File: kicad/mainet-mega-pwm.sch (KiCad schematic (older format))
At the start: 0 parts

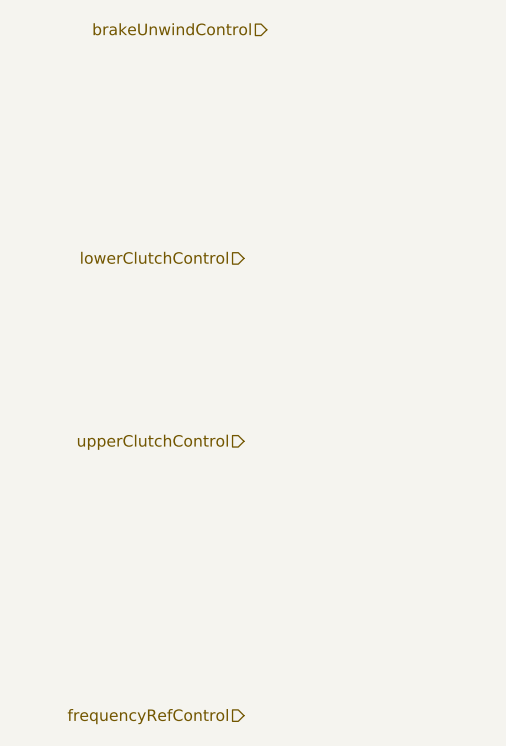
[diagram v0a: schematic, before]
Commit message: Kicad: Modificaciones menores esquemáticos
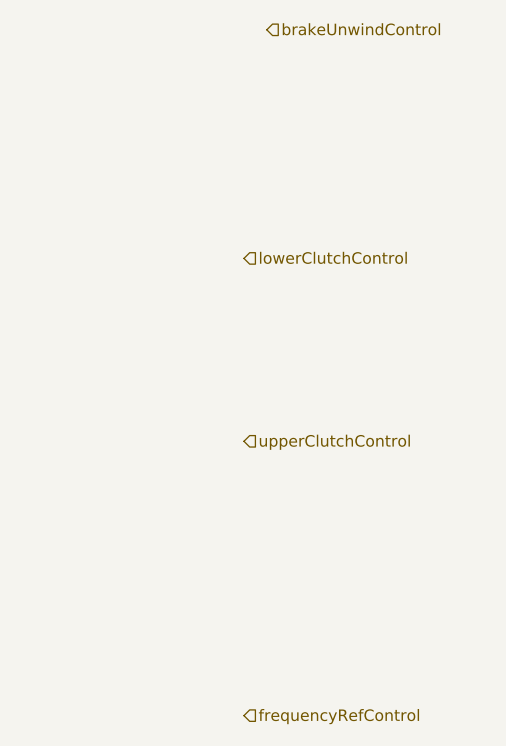
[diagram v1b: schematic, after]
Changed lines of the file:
@@
 $Descr A4 11693 8268
 encoding utf-8
-Sheet 3 17
+Sheet 17 17
 Title ""
 Date ""
@@
 Comment4 ""
 $EndDescr
-Text HLabel 2350 1700 0    50   Input ~ 0
+Text HLabel 2350 1700 2    50   Input ~ 0
 brakeUnwindControl
-Text HLabel 2250 2700 0    50   Input ~ 0
+Text HLabel 2250 2700 2    50   Input ~ 0
 lowerClutchControl
-Text HLabel 2250 3500 0    50   Input ~ 0
+Text HLabel 2250 3500 2    50   Input ~ 0
 upperClutchControl
-Text HLabel 2250 4700 0    50   Input ~ 0
+Text HLabel 2250 4700 2    50   Input ~ 0
 frequencyRefControl
 $EndSCHEMATC

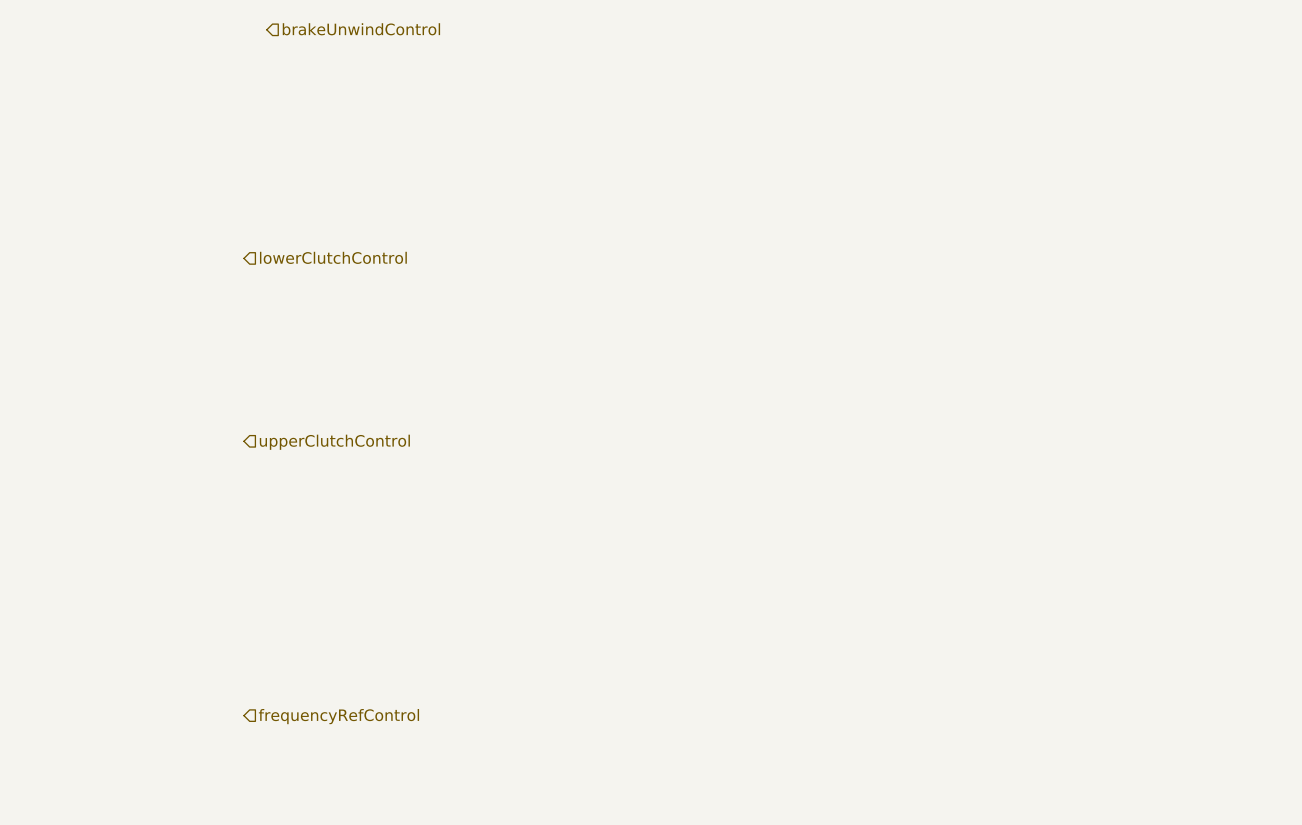
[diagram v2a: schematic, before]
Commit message: KiCAD: Se agregó esquemáticos del módulo de coversión de voltaje de 5V a !0 V
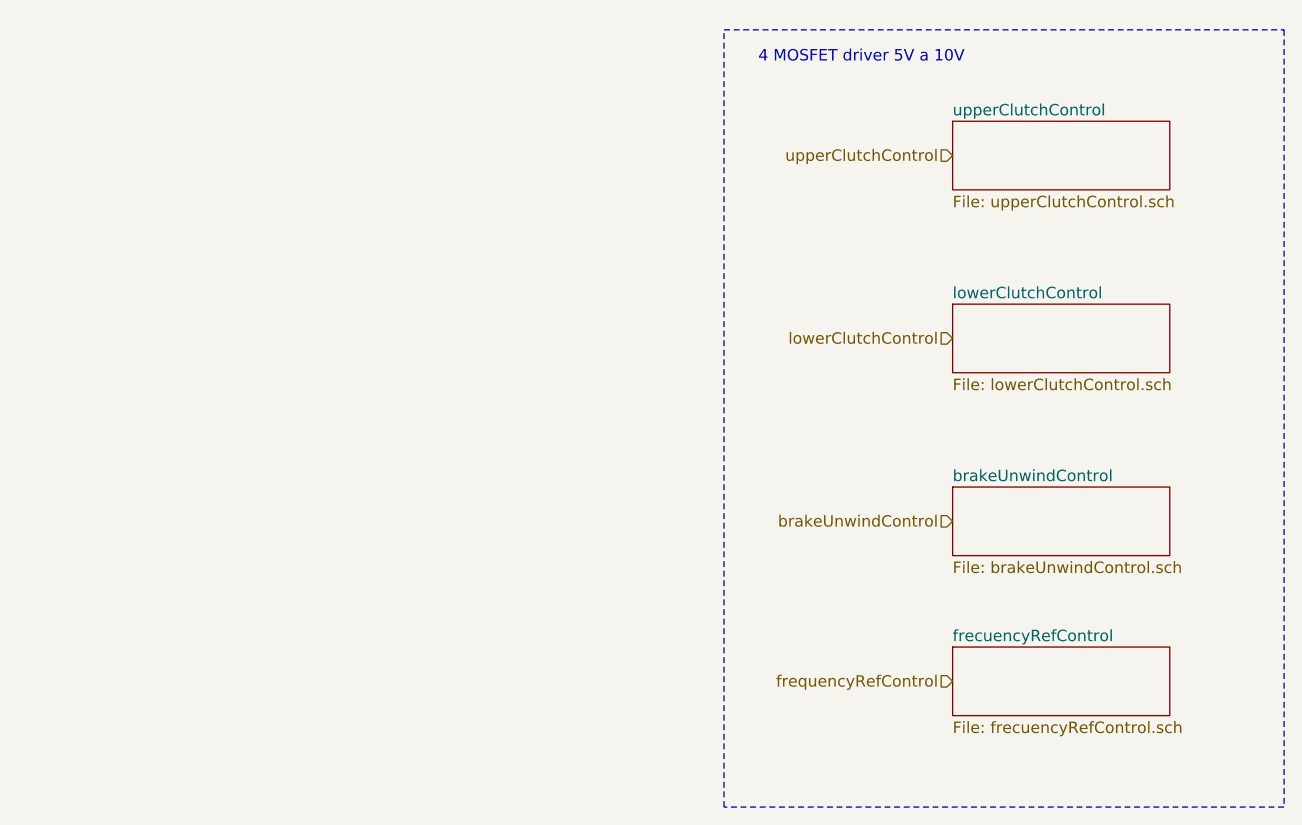
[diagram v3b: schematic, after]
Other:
- note added: "4 MOSFET driver 5V a 10V"
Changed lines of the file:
@@
 EESchema Schematic File Version 4
 LIBS:mainet-mega-cache
-LIBS:mainet-mega-rotary-pulse-generator-24v-to-mega-5v-cache
+LIBS:mainet-mega-5V-to-mp-10v-cache
 EELAYER 30 0
 EELAYER END
 $Descr A4 11693 8268
 encoding utf-8
-Sheet 17 17
+Sheet 15 21
 Title ""
 Date ""
@@
 Comment4 ""
 $EndDescr
-Text HLabel 2350 1700 2    50   Input ~ 0
+Text HLabel 5350 3850 0    50   Input ~ 0
 brakeUnwindControl
-Text HLabel 2250 2700 2    50   Input ~ 0
+Text HLabel 5350 3050 0    50   Input ~ 0
 lowerClutchControl
-Text HLabel 2250 3500 2    50   Input ~ 0
+Text HLabel 5350 2250 0    50   Input ~ 0
 upperClutchControl
-Text HLabel 2250 4700 2    50   Input ~ 0
+Text HLabel 5350 4550 0    50   Input ~ 0
 frequencyRefControl
+$Sheet
+S 5350 2100 950  300
+U 601ACD13
+F0 "upperClutchControl" 50
+F1 "upperClutchControl.sch" 50
+$EndSheet
+$Sheet
+S 5350 2900 950  300
+U 601BF406
+F0 "lowerClutchControl" 50
+F1 "lowerClutchControl.sch" 50
+$EndSheet
+$Sheet
+S 5350 4400 950  300
+U 601C4CB6
+F0 "frecuencyRefControl" 50
+F1 "frecuencyRefControl.sch" 50
+$EndSheet
+$Sheet
+S 5350 3700 950  300
+U 601CE166
+F0 "brakeUnwindControl" 50
+F1 "brakeUnwindControl.sch" 50
+$EndSheet
+Wire Notes Line
+	4350 1700 6800 1700
+Wire Notes Line
+	6800 1700 6800 5100
+Wire Notes Line
+	6800 5100 4350 5100
+Wire Notes Line
+	4350 5100 4350 1700
+Text Notes 4500 1850 0    50   ~ 0
+4 MOSFET driver 5V a 10V
 $EndSCHEMATC
